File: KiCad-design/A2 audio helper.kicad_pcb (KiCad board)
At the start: 2 copper layers, 45 x 83.5 mm, 37 parts, among them J1 PIN HEADER 1x2, J10 PIN HEADER 1x2, J11 PIN HEADER 1x3, J12 PIN HEADER 1x3, J13 PIN HEADER 2x4, J15 PIN HEADER 2x6, J16 PIN HEADER 2x6, J17 SJ1-3515N, J3 PIN HEADER 1x2, J4 SJ1-3515N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

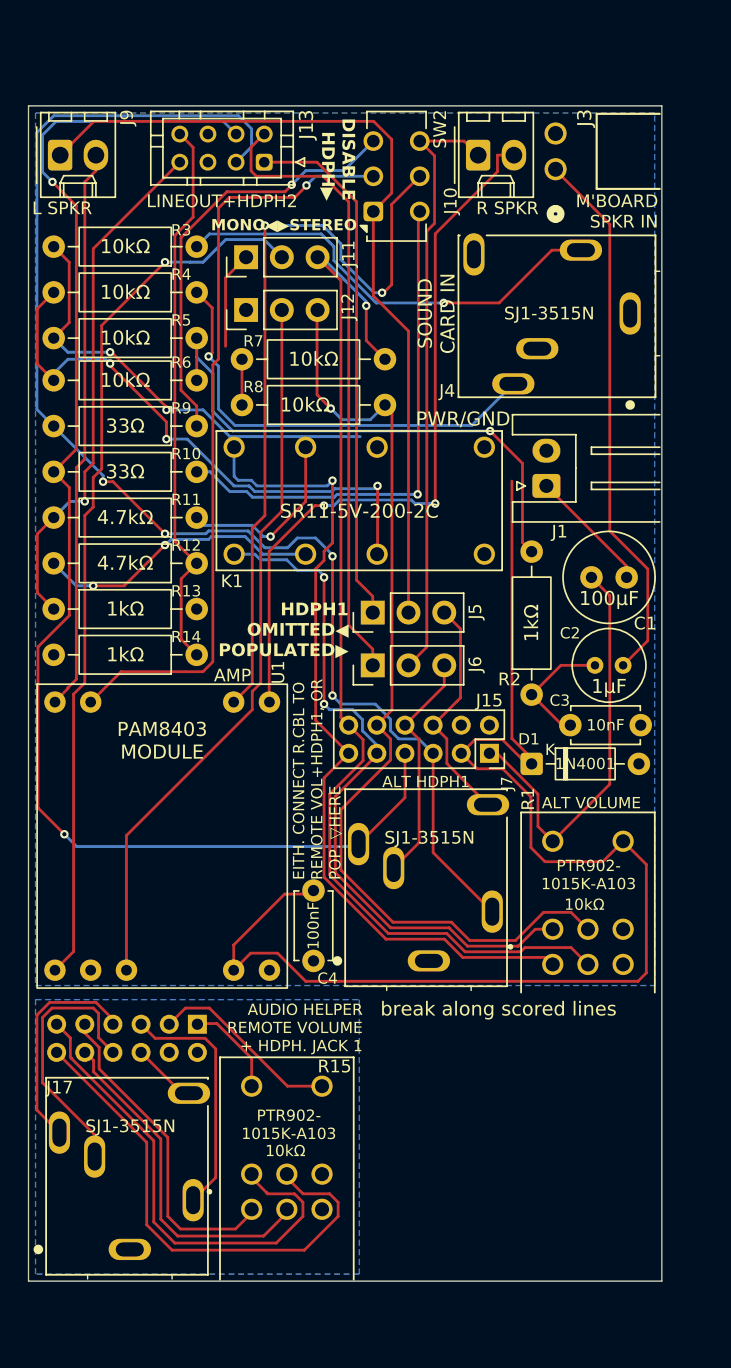
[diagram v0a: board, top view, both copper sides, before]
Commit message: picked new part for front hp jack
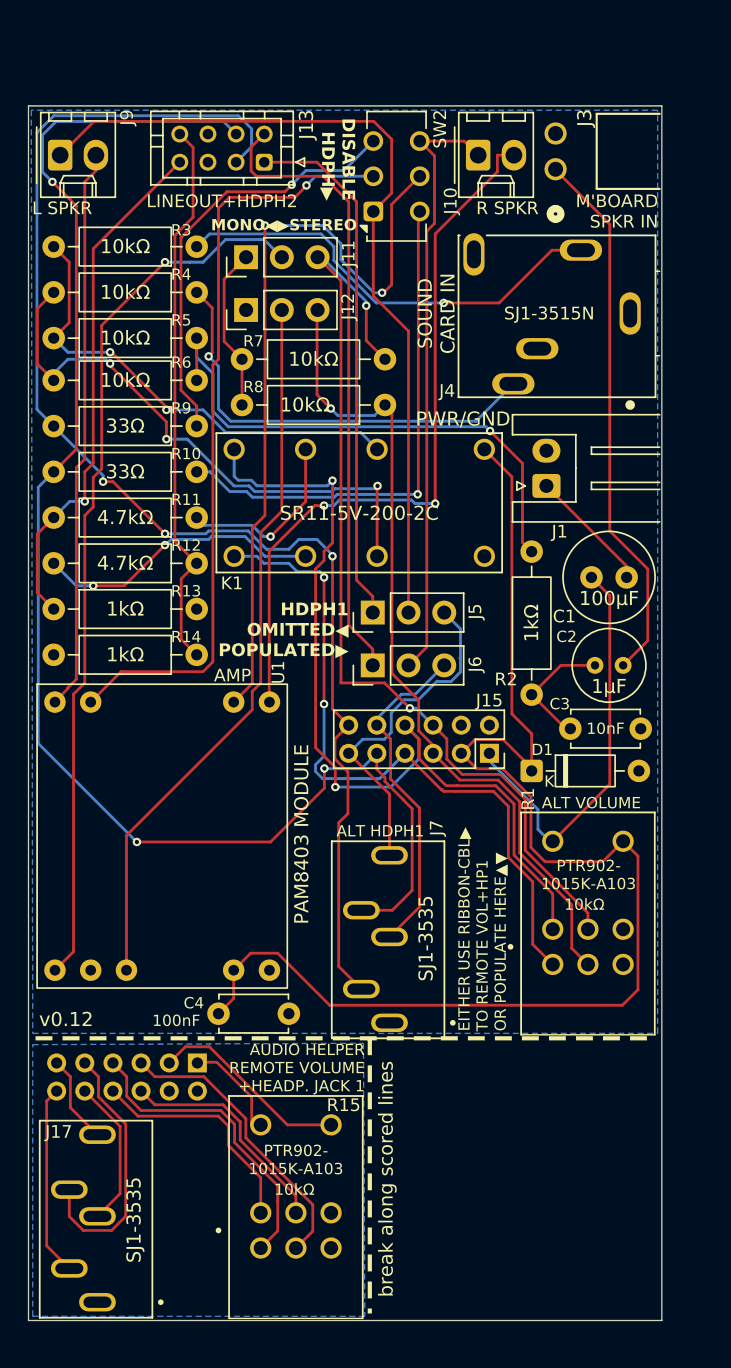
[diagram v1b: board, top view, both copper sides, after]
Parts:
- J17, J7: value SJ1-3515N -> SJ1-3535; footprint SJ1-3515N:CUI_SJ1-3515N -> SJ1-3535:CUI_SJ1-3535
- moved C4 11.1 mm to (63.5, 100.5), turned to 0 degrees
- moved J7 5.22 mm to (75.7, 101.2)
- moved J17 4.40 mm to (54.9, 121.0)
- moved R15 2.82 mm to (69.0, 122.2)
- moved J16 2.75 mm to (62.0, 104.0)
- moved D1 0.50 mm to (85.8, 83.2)
- moved C3 0.25 mm to (88.5, 80.2)
- moved K1 0.15 mm to (73.5, 64.2)
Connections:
- J10 pad 2: /SPKR_R -> Net-(J10-Pin_2)
- J15 pad 10: VOL_R -> HP1_RN
- J15 pad 11: SRC_L -> HP1_TN
- J15 pad 12: VOL_L -> HP1_T
- J15 pad 5: HP1_T -> VOL_R
- J15 pad 6: HP1_TN -> VOL_L
- J15 pad 7: HP1_R -> SRC_R
- J15 pad 8: HP1_RN -> SRC_L
- J15 pad 9: SRC_R -> HP1_R
- J16 pad 10: /Daughterboard/REM_VOL_R -> /Daughterboard/RMT_HP1_RN
- J16 pad 11: /Daughterboard/RMT_SRC_L -> /Daughterboard/RMT_HP1_TN
- J16 pad 12: /Daughterboard/REM_VOL_L -> /Daughterboard/RMT_HP1_T
- J16 pad 5: /Daughterboard/RMT_HP1_T -> /Daughterboard/REM_VOL_R
- J16 pad 6: /Daughterboard/RMT_HP1_TN -> /Daughterboard/REM_VOL_L
- J16 pad 7: /Daughterboard/RMT_HP1_R -> /Daughterboard/RMT_SRC_R
- J16 pad 8: /Daughterboard/RMT_HP1_RN -> /Daughterboard/RMT_SRC_L
- J16 pad 9: /Daughterboard/RMT_SRC_R -> /Daughterboard/RMT_HP1_R
- J9 pad 2: /SPKR_L -> Net-(J9-Pin_2)
- U1 pad 6: /SPKR_R -> Net-(J10-Pin_2)
- U1 pad 9: /SPKR_L -> Net-(J9-Pin_2)
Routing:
- net Net-(J10-Pin_2): track 0.00 -> 51.8 mm, vias 0 -> 2
- net /SPKR_R: track 94.8 -> 43.0 mm, vias 2 -> 0
- net Net-(J9-Pin_2): track 0.00 -> 40.1 mm
- net /SPKR_L: track 100.3 -> 60.3 mm
- net /Daughterboard/REM_VOL_L: track 35.6 -> 16.0 mm
- net /Daughterboard/RMT_SRC_L: track 34.3 -> 16.3 mm
- net VOL_R: track 68.8 -> 59.4 mm
- net /Daughterboard/RMT_HP1_RN: track 19.0 -> 10.6 mm
- net HP1_R: track 96.8 -> 105.0 mm, vias 2 -> 3
- net VOL_L: track 76.9 -> 68.8 mm, vias 1 -> 2
- net HP1_TN: track 16.5 -> 24.4 mm
- net HP1_RN: track 16.8 -> 24.0 mm
- net SRC_L: track 58.7 -> 62.7 mm, vias 1 -> 2
- net /Daughterboard/RMT_HP1_T: track 17.5 -> 13.6 mm
- net /Daughterboard/REM_VOL_R: track 24.3 -> 20.7 mm
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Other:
- board size 45 x 83.5 mm -> 45 x 86.3 mm
- board text added: "AUDIO HELPER REMOTE VOLUME +HEADP. JACK 1"
- board text added: "Apple 2 Audio Helper v0.12"
- board text added: "EITHER USE RIBBON-CBL▶ TO REMOTE ︎VOL+HP1 OR POPULATE HERE▲▼"
- board text added: "v0.12"
- board text removed: "AUDIO HELPER REMOTE VOLUME + HDPH. JACK 1"
- board text removed: "Apple 2 Audio Helper v0.10.3"
- board text removed: "EITH. CONNECT R.CBL TO REMOTE VOL+HDPH1, OR POP. ▽HERE"

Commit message: lengthened, new bigger switch part, cleanup
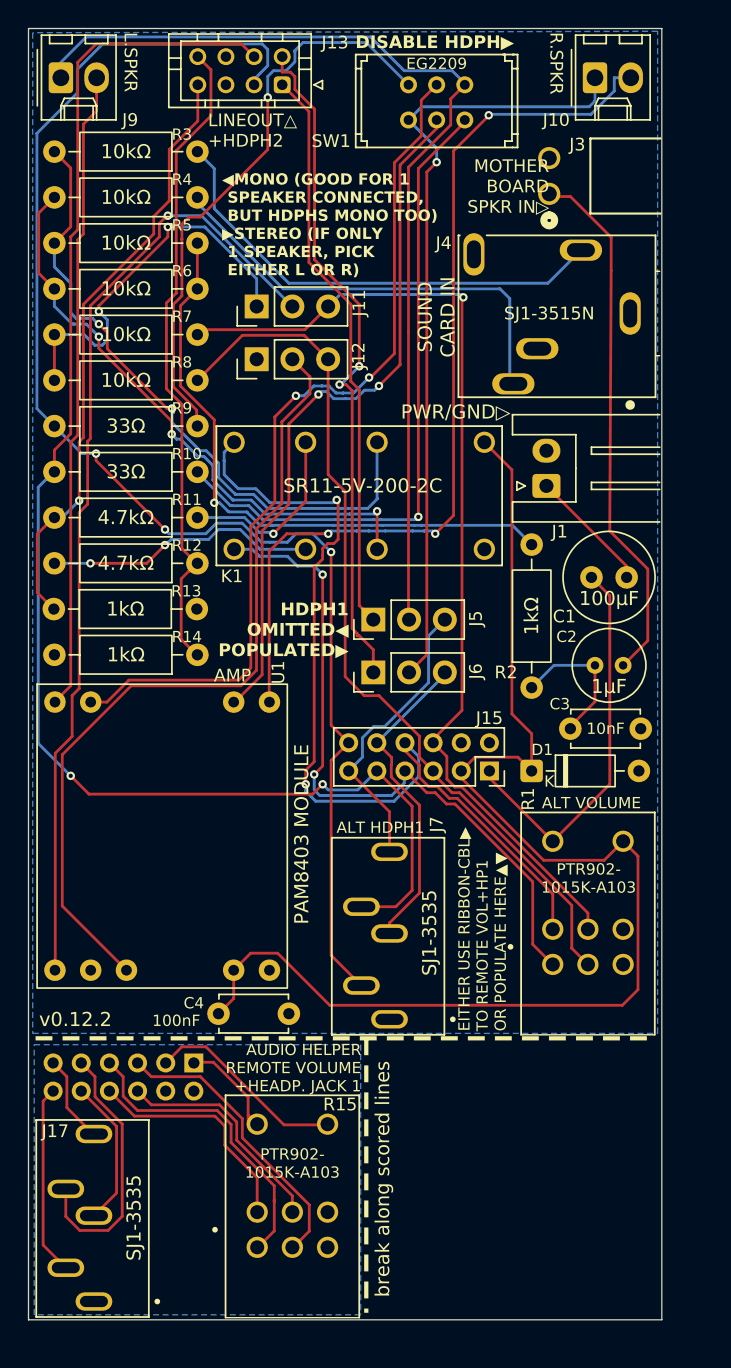
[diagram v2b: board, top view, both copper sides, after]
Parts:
- removed SW2: SW_DPDT_x2, Button_Switch_THT:SW_CK_JS202011CQN_DPDT_Straight
- added SW1: EG2209, EG2209:EG2209, F.Cu at (77.0, 34.5)
- J1: value PIN HEADER 1x2 -> S2B-XH-A
- J10, J9: value PIN HEADER 1x2 -> AE-6410-2A
- J13: value PIN HEADER 2x4 -> JST B8B-PHDSS
- J3: value PIN HEADER 1x2 -> 22053021
- moved R7 13.4 mm to (62.0, 52.2)
- moved R8 13.4 mm to (62.0, 55.5)
- moved J10 9.96 mm to (90.2, 34.0)
- moved R3 6.75 mm to (62.0, 39.2)
- moved R4 6.75 mm to (62.0, 42.5)
- moved R5 6.75 mm to (62.0, 45.8)
- moved R6 6.50 mm to (62.0, 49.0)
- moved J13 5.65 mm to (68.0, 34.5)
- moved J9 5.50 mm to (52.3, 34.0)
- moved J11 3.58 mm to (66.2, 50.2)
- moved J12 3.58 mm to (66.2, 54.0)
- moved J3 1.81 mm to (87.0, 42.2)
- moved J15 1.25 mm to (82.8, 83.2)
- moved J5 0.50 mm to (74.5, 72.5)
- moved J6 0.50 mm to (74.5, 76.2)
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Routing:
- net /MONO_MIX: track 11.7 -> 27.6 mm, vias 0 -> 2
- net Net-(J10-Pin_2): track 51.8 -> 66.3 mm, vias 2 -> 3
- net /SPKR_R: track 43.0 -> 56.2 mm, vias 0 -> 1
- net /INPUT_AUDIO_L: track 33.8 -> 46.6 mm
- net Net-(R9-Pad1): track 30.4 -> 41.6 mm
- net /SPKR_L: track 60.3 -> 71.2 mm
- net Net-(R10-Pad1): track 36.6 -> 46.8 mm
- net Net-(U1-L+): track 54.2 -> 62.0 mm, vias 1 -> 2
- net /LINEOUT_R: track 39.5 -> 46.9 mm
- net /LINEOUT_L: track 37.0 -> 43.6 mm
- net /AMP_INPUT_R: track 51.5 -> 57.7 mm
- net Net-(J9-Pin_2): track 40.1 -> 45.6 mm
- net /AMP_INPUT_L: track 63.0 -> 68.5 mm
- net Net-(U1-R+): track 55.2 -> 50.0 mm
- net /AUDIO_MB_AC: track 38.7 -> 43.7 mm
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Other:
- board size 45 x 86.3 mm -> 45 x 91.8 mm
- board text added: "100nF"
- board text added: "100µF"
- board text added: "10kΩ"
- board text added: "10nF"
- board text added: "1kΩ"
- board text added: "1µF"
- board text added: "33Ω"
- board text added: "4.7kΩ"
- board text added: "Apple 2 Audio Helper v0.12.2"
- board text added: "EG2209"
- board text added: "L.SPKR"
- board text added: "LINEOUT△ +HDPH2"
- board text added: "MOTHER BOARD SPKR IN▷"
- board text added: "PWR/GND▷"
- board text added: "R.SPKR"
- board text added: "SJ1-3515N"
- board text added: "SJ1-3535"
- board text added: "SR11-5V-200-2C"
- board text added: "v0.12.2"
- board text added: "◀︎MONO (GOOD FOR 1 SPEAKER CONNECTED, BUT HDPHS MONO TOO) ▶︎STEREO (IF ONLY 1 SPEAKER, PICK EITHER L OR R)"
- board text removed: "Apple 2 Audio Helper v0.12"
- board text removed: "L SPKR"
- board text removed: "LINEOUT+HDPH2"
- board text removed: "M'BOARD SPKR IN"
- board text removed: "MONO◀︎▶︎STEREO"
- board text removed: "PWR/GND"
- board text removed: "R SPKR"
- board text removed: "v0.12"

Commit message: pcb mount holes, add missing component files
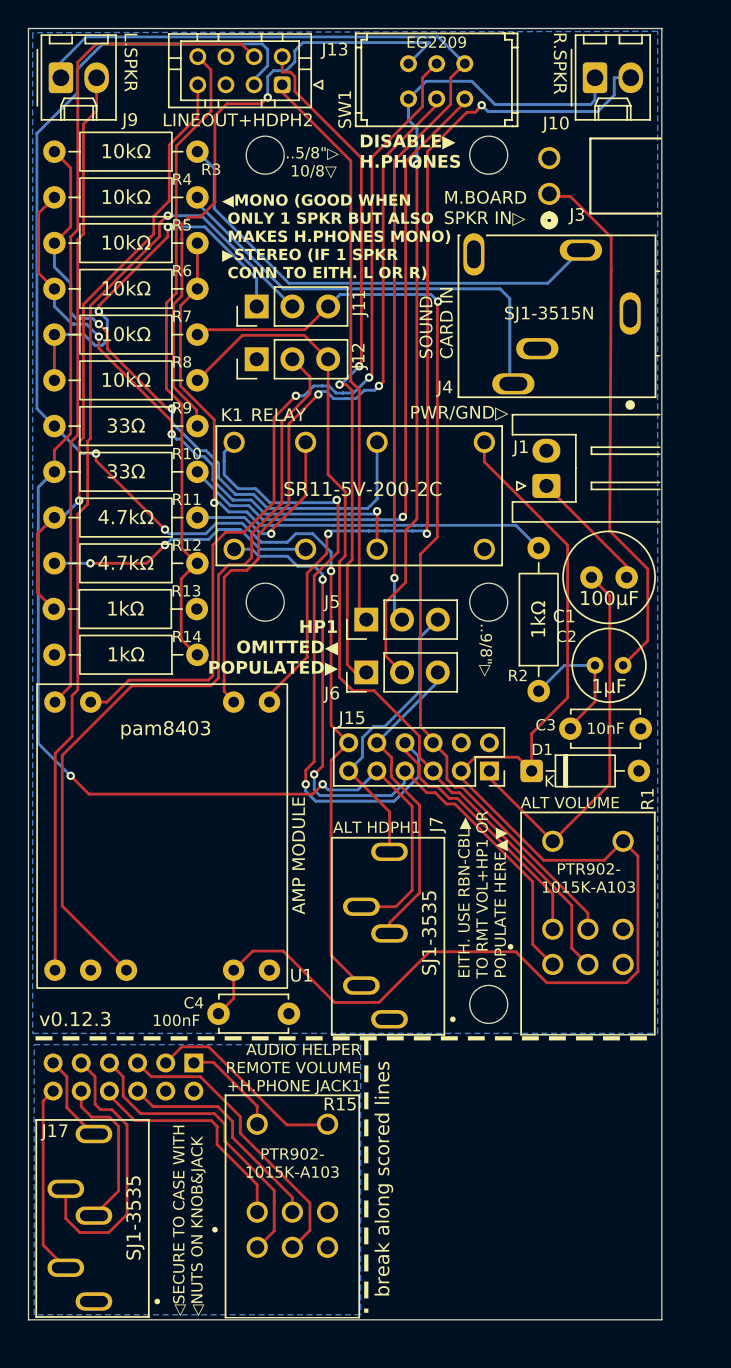
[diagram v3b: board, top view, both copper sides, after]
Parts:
- added REF**: MountingHole_2.7mm_M2.5, MountingHole:MountingHole_2.7mm_M2.5, F.Cu at (82.7, 39.5)
- added REF**: MountingHole_2.7mm_M2.5, MountingHole:MountingHole_2.7mm_M2.5, F.Cu at (66.8, 71.3)
- added REF**: MountingHole_2.7mm_M2.5, MountingHole:MountingHole_2.7mm_M2.5, F.Cu at (82.7, 99.8)
- added REF**: MountingHole_2.7mm_M2.5, MountingHole:MountingHole_2.7mm_M2.5, F.Cu at (66.8, 39.5)
- added REF**: MountingHole_2.7mm_M2.5, MountingHole:MountingHole_2.7mm_M2.5, F.Cu at (82.7, 71.3)
- moved SW1 1.50 mm to (77.0, 33.0)
- moved R2 0.56 mm to (86.2, 77.6)
- moved J5 0.50 mm to (74.0, 72.5)
- moved J6 0.50 mm to (74.0, 76.2)
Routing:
- net Net-(R9-Pad1): track 41.6 -> 45.4 mm
- net V_AMP: track 91.5 -> 94.6 mm
- net Net-(U1-R+): track 50.0 -> 52.8 mm
- net /SPKR_L: track 71.2 -> 73.3 mm, vias 0 -> 1
- net VOL_L: track 70.8 -> 68.8 mm
- net /SPKR_R: track 56.2 -> 58.1 mm
- net /Daughterboard/RMT_HP1_R: track 18.9 -> 20.0 mm
- net /HP2_RN: track 48.4 -> 49.4 mm
- net Net-(U1-L+): track 62.0 -> 63.0 mm
- net Net-(R10-Pad1): track 46.8 -> 47.7 mm
- net /Daughterboard/RMT_HP1_RN: track 10.6 -> 11.4 mm
- net /Daughterboard/RMT_V_IN: track 7.82 -> 7.12 mm
- net /AMP_INPUT_R: track 57.7 -> 57.0 mm
- net VOL_R: track 63.3 -> 64.0 mm
- net /AUDIO_MB_AC: track 43.7 -> 44.3 mm
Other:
- board text added: "..5/8{dblquote}▷ 10/8▽"
- board text added: "..9/8{dblquote}▷"
- board text added: "AMP MODULE"
- board text added: "AUDIO HELPER REMOTE VOLUME +H.PHONE JACK1"
- board text added: "EITH. USE RBN-CBL▶ TO RMT ︎VOL+HP1 OR POPULATE HERE▲▼"
- board text added: "HP1 OMITTED◀ POPULATED▶ ︎"
- board text added: "LINEOUT+HDPH2"
- board text added: "M.BOARD SPKR IN▷"
- board text added: "RELAY"
- board text added: "making board a bit larger would allow another mounting hole in this corner"
- board text added: "v0.12.3"
- board text added: "◀︎MONO (GOOD WHEN ONLY 1 SPKR BUT ALSO MAKES H.PHONES MONO) ▶︎STEREO (IF 1 SPKR CONN TO EITH. L OR R)"
- board text added: "◁SECURE TO CASE WITH ◁NUTS ON KNOB&JACK"
- board text added: "︎︎DISABLE▶ H.PHONES"
- board text removed: "AMP"
- board text removed: "AUDIO HELPER REMOTE VOLUME +HEADP. JACK 1"
- board text removed: "EITHER USE RIBBON-CBL▶ TO REMOTE ︎VOL+HP1 OR POPULATE HERE▲▼"
- board text removed: "HDPH1 OMITTED◀ POPULATED▶ ︎"
- board text removed: "LINEOUT△ +HDPH2"
- board text removed: "MOTHER BOARD SPKR IN▷"
- board text removed: "PAM8403 MODULE"
- board text removed: "v0.12.2"
- board text removed: "◀︎MONO (GOOD FOR 1 SPEAKER CONNECTED, BUT HDPHS MONO TOO) ▶︎STEREO (IF ONLY 1 SPEAKER, PICK EITHER L OR R)"
- board text removed: "︎︎DISABLE HDPH▶"
